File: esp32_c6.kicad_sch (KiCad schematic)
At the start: 1 part, among them U1 ESP32-WROOM-32

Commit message: ESP32S3 branch initial changes
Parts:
- removed U1: ESP32-WROOM-32, RF_Module:ESP32-WROOM-32, symbol RF_Module:ESP32-WROOM-32
- added C11, C3, C4: 100nf, Capacitor_SMD:C_0805_2012Metric, symbol Device:C
- added U1: ESP32-C6-DEVKITC-1-N8, kiC:MODULE_ESP32-C6-DEVKITC-1-N8, symbol ESP32-C6-DEVKITC-1-N8:ESP32-C6-DEVKITC-1-N8
- added U9: ESP32-C6-WROOM-1-N8, kiC:XCVR_ESP32-C6-WROOM-1-N8, symbol ESP32-C6-DEVKITC-1-N8:ESP32-C6-WROOM-1-N8
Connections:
- new net +3V3: C11.1, C3.1, C4.1, U1.J1_1 (ESP_3V3), U9.2 (3V3)
- new net +5V: U1.J1_14 (VCC_5V)
- new net EN: U1.J1_2 (CHIP_PU), U9.3 (EN)
- new net GND: C11.2, C3.2, C4.2, U1.J1_15 (GND_J1_15), U1.J3_1 (GND_J3_1), U1.J3_12 (GND_J3_12), U1.J3_15 (GND_J3_15), U9.1 (GND), U9.28 (GND), U9.29_1 (GND), U9.29_2 (GND), U9.29_3 (GND), U9.29_4 (GND), U9.29_5 (GND), U9.29_6 (GND), U9.29_7 (GND), U9.29_8 (GND), U9.29_9 (GND)
- new net IO_0: U1.J1_7 (GPIO0), U9.8 (IO0)
- new net IO_1: U1.J1_8 (GPIO1), U9.9 (IO1)
- new net IO_10: U1.J1_10 (GPIO10), U9.11 (IO10)
- new net IO_11: U1.J1_11 (GPIO11), U9.12 (IO11)
- new net IO_12: U1.J3_14 (GPIO12), U9.13 (IO12)
- new net IO_13: U1.J3_13 (GPIO13), U9.14 (IO13)
- new net IO_15: U1.J3_4 (GPIO15), U9.23 (IO15)
- new net IO_16: U9.25 (TXD0/GPIO16)
- new net IO_17: U9.24 (RXD0/GPIO17)
- new net IO_18: U1.J3_10 (GPIO18), U9.16 (IO18)
- new net IO_19: U1.J3_9 (GPIO19), U9.17 (IO19)
- new net IO_2: U1.J1_12 (GPIO2), U9.27 (IO2)
- new net IO_20: U1.J3_8 (GPIO20), U9.18 (IO20)
- new net IO_21: U1.J3_7 (GPIO21), U9.19 (IO21)
- new net IO_22: U1.J3_6 (GPIO22), U9.20 (IO22)
- new net IO_23: U1.J3_5 (GPIO23), U9.21 (IO23)
- new net IO_3: U1.J1_13 (GPIO3), U9.26 (IO3)
- new net IO_4: U1.J1_3 (GPIO4), U9.4 (IO4)
- new net IO_5: U1.J1_4 (GPIO5), U9.5 (IO5)
- new net IO_6: U1.J1_5 (GPIO6), U9.6 (IO6)
- new net IO_7: U1.J1_6 (GPIO7), U9.7 (IO7)
- new net IO_8: U1.J1_9 (GPIO8), U9.10 (IO8)
- new net IO_9: U1.J3_11 (GPIO9), U9.15 (IO9)
- new net MRX: U1.J3_3 (UART_RXD)
- new net MTX: U1.J3_2 (UART_TXD)

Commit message: Update KiCad project files
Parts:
- renumbered C3 to C1, C4 to C2, C11 to C3, U9 to U1, U1 to U2
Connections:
- net MRX is gone; now on net RXD0: U2.J3_3 (UART_RXD)
- net MTX is gone; now on net TXD0: U2.J3_2 (UART_TXD)
- net IO_16 renamed TXD0
- net IO_17 renamed RXD0
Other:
- moved on the sheet: C3, U1, U2

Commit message: Remove unused schematic files, lock files, and backup directories
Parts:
- added C10, C13, C14: 100n, Capacitor_SMD:C_0805_2012Metric, symbol Device:C
- added D10, D11, D9: LESD5D5.0CT1G, clackotron_fp:SOD-523_L1.2-W0.8-LS1.6-BI, symbol clackotronlib:LESD5D5.0CT1G
- added D12: ESD3.3, Diode_SMD:D_SOD-923, symbol Diode:ESD9B3.3ST5G
- added D8: 1N4148W, Diode_SMD:D_SOD-123, symbol Diode:1N4148W
- added J6: FT232RL, Connector_PinHeader_2.54mm:PinHeader_1x06_P2.54mm_Vertical, symbol Connector:Conn_01x06_Pin
- added Q4, Q5: Q_NPN_BCE, Package_TO_SOT_SMD:SOT-23W, symbol Device:Q_NPN_BCE
- added R15, R16, R20: 10k, Resistor_SMD:R_0805_2012Metric, symbol Device:R
- added R58, R59: 5.1k, Resistor_SMD:R_0805_2012Metric, symbol Device:R
- added SW1, SW2: SW_Push, Button_Switch_SMD:SW_Push_SPST_NO_Alps_SKRK, symbol Switch:SW_Push
- added SW11: boot, Button_Switch_SMD:SW_SPST_B3U-1000P, symbol Switch:SW_SPST
- added USBC1: USB3.1C16PFSMT, clackotron_fp:USB-C-SMD_TYPE-C-USB-17, symbol clackotronlib:USB3.1C16PFSMT
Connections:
- net +3V3: now also D8.1 (K)
- net EN: now also C10.1, C14.1, Q4.2 (C), R20.2, SW1.2
- net GND: now also C10.2, C13.2, C14.2, D10.1, D11.1, D12.1 (A1), D9.1, J6.6 (Pin_6), R58.1, R59.2, SW1.1, SW11.1 (A), SW2.1, USBC1.0, USBC1.A1 (GND), USBC1.A12 (GND)
- net IO_0: now also Q5.2 (C)
- net RXD0: now also J6.2 (Pin_2)
- net TXD0: now also J6.3 (Pin_3)
- new net: D8.2 (A), J6.4 (Pin_4)
- new net: Q5.1 (B), R16.2
- new net: R59.1, USBC1.A5 (CC1)
- new net: Q4.1 (B), R15.2
- new net: R58.2, USBC1.B5 (CC2)
- new net: D12.2 (A2), SW11.2 (B)
- new net +3.3V: R20.1
- new net CTS: J6.5 (Pin_5), Q4.3 (E), R16.1
- new net DTR: J6.1 (Pin_1), Q5.3 (E), R15.1
- new net GPIO0: C13.1, SW2.2
- new net USB2_D+: D10.2, USBC1.A7 (DN1), USBC1.B6 (DP2)
- new net USB2_D-: D9.2, USBC1.A6 (DP1), USBC1.B7 (DN2)
- new net VBUS: D11.2, USBC1.A4 (VBUS), USBC1.A9 (VBUS)
- no-connect marks 0 -> 2
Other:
- note added: "Automatic Bootloader"
- moved on the sheet: C1, C2, C3, U1, U2

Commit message: Update all schematic files and project
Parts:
- added C45, C46: 100nf, Capacitor_SMD:C_0805_2012Metric, symbol Device:C
- added J21: USB_B_Mini, kiC:USB_Mini-B_Lumberg_2486_01_Horizontal, symbol Connector:USB_B_Mini
- added L7: 100mh, Inductor_SMD:L_1206_3216Metric, symbol Device:L
- added R26, R37: 27, Resistor_SMD:R_0805_2012Metric, symbol Device:R
- added R62, R63: 5.1k, Resistor_SMD:R_0805_2012Metric, symbol Device:R
- added U9: LM1117DT-3.3, kiC:SOT-223-3_TabPin2, symbol Regulator_Linear:LM1117DT-3.3
- D10, D11, D9: footprint clackotron_fp:SOD-523_L1.2-W0.8-LS1.6-BI -> Diode_SMD:D_SOD-523
- SW11: footprint Button_Switch_SMD:SW_SPST_B3U-1000P -> Button_Switch_SMD:SW_Push_SPST_NO_Alps_SKRK
- USBC1: footprint clackotron_fp:USB-C-SMD_TYPE-C-USB-17 -> kiC:USB-C-SMD_TYPE-C-USB-17
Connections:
- net +3V3: now also C46.2, U9.2 (VO)
- net GND: now also C45.1, C46.1, J21.5 (GND1), J21.6 (Shield), U9.1 (GND1)
- net IO_12: now also R37.1, R63.1
- net IO_13: now also R26.1, R62.1
- net USB2_D+: now also R62.2
- net USB2_D-: now also R63.2
- net VBUS: now also J21.1 (VBUS), L7.1
- net GPIO9: now reaches D12.2 (A2), SW11.2 (B)
- new net: J21.2 (D-), R37.2
- new net: J21.3 (D+), R26.2
- new net: C45.2, L7.2, U9.3 (VI)
- new net ID_USB: J21.4 (ID)
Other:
- moved on the sheet: D11, D12, SW11

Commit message: Update all schematic files and project
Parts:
- removed SW2: SW_Push, Button_Switch_SMD:SW_Push_SPST_NO_Alps_SKRK, symbol Switch:SW_Push
- added C49: 100nf, Capacitor_SMD:C_1206_3216Metric, symbol Device:C
- added C50, C51: 100n, Capacitor_SMD:C_0805_2012Metric, symbol Device:C
- added D14: 1N5819, Diode_SMD:D_2512_6332Metric, symbol Diode:1N5819
- added J22: JTAG, Connector_PinHeader_1.27mm:PinHeader_1x06_P1.27mm_Vertical, symbol Connector:Conn_01x06_Pin
- added R64: 10K, Resistor_SMD:R_0805_2012Metric, symbol Device:R
- added Y2: Crystal, Crystal:Crystal_SMD_EuroQuartz_EQ161-2Pin_3.2x1.5mm, symbol Device:Crystal
- C45: footprint Capacitor_SMD:C_0805_2012Metric -> Capacitor_SMD:C_1206_3216Metric
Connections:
- net GPIO0 is gone; now on net GPIO9: C13.1
- net +3V3: now also J22.1 (Pin_1), R64.1
- net +5V: now also C45.2, L7.2, U9.3 (VI), C49.2
- net GND: now also C49.1, C50.2, C51.2, J22.6 (Pin_6)
- net IO_0: now also C50.1, Y2.1
- net IO_1: now also C51.1, Y2.2
- net IO_4: now also J22.2 (Pin_2)
- net IO_5: now also J22.3 (Pin_3)
- net IO_6: now also J22.4 (Pin_4)
- net IO_7: now also J22.5 (Pin_5)
- net IO_8: now also R64.2
- net VBUS: now also D14.2 (A); no longer L7.1
- new net: D14.1 (K), L7.1
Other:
- moved on the sheet: D12, SW11, U1, U2

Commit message: Update schematics, PCB, and project files
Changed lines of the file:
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@@
 		(color 0 0 0 0)
 	)
-	(junction
-		(at 64.77 119.38)
-		(diameter 0)
-		(color 0 0 0 0)
-	)
 	(no_connect
 		(at 113.665 50.8)
@@
 	(wire
 		(pts
-			(xy 62.23 119.38) (xy 64.77 119.38)
-		)
-		(stroke
-			(width 0)
-			(type default)
-		)
-	)
-	(wire
-		(pts
 			(xy 228.6 219.71) (xy 240.03 219.71)
 		)
@@
 	(wire
 		(pts
-			(xy 246.38 93.98) (xy 243.84 93.98)
-		)
-		(stroke
-			(width 0)
-			(type default)
-		)
-	)
-	(wire
-		(pts
 			(xy 84.455 53.34) (xy 84.455 59.69)
 		)
@@
 	(wire
 		(pts
-			(xy 64.77 116.84) (xy 64.77 119.38)
+			(xy 133.35 209.55) (xy 133.35 210.82)
 		)
 		(stroke
@@
 	(wire
 		(pts
-			(xy 133.35 209.55) (xy 133.35 210.82)
+			(xy 246.38 147.32) (xy 243.84 147.32)
 		)
 		(stroke
@@
 	(wire
 		(pts
-			(xy 246.38 147.32) (xy 243.84 147.32)
+			(xy 91.44 168.91) (xy 105.41 168.91)
 		)
 		(stroke
@@
 	(wire
 		(pts
-			(xy 91.44 168.91) (xy 105.41 168.91)
+			(xy 142.24 58.42) (xy 142.24 60.96)
 		)
 		(stroke
@@
 	(wire
 		(pts
-			(xy 142.24 58.42) (xy 142.24 60.96)
+			(xy 354.33 199.39) (xy 354.33 203.2)
 		)
 		(stroke
@@
 	(wire
 		(pts
-			(xy 354.33 200.66) (xy 354.33 203.2)
+			(xy 127 133.35) (xy 148.59 133.35)
 		)
 		(stroke
@@
 	(wire
 		(pts
-			(xy 127 133.35) (xy 148.59 133.35)
+			(xy 64.77 116.84) (xy 64.77 121.92)
 		)
 		(stroke
@@
 	(wire
 		(pts
-			(xy 62.23 116.84) (xy 62.23 119.38)
+			(xy 62.23 116.84) (xy 62.23 123.19)
 		)
 		(stroke
@@
 	(wire
 		(pts
-			(xy 246.38 129.54) (xy 243.84 129.54)
-		)
-		(stroke
-			(width 0)
-			(type default)
-		)
-	)
-	(wire
-		(pts
 			(xy 130.81 209.55) (xy 133.35 209.55)
 		)
@@
 	(wire
 		(pts
-			(xy 246.38 127) (xy 243.84 127)
-		)
-		(stroke
-			(width 0)
-			(type default)
-		)
-	)
-	(wire
-		(pts
 			(xy 82.55 101.6) (xy 72.39 101.6)
 		)
@@
 	(wire
 		(pts
-			(xy 64.77 119.38) (xy 64.77 121.92)
-		)
-		(stroke
-			(width 0)
-			(type default)
-		)
-	)
-	(wire
-		(pts
 			(xy 144.78 128.27) (xy 148.59 128.27)
 		)
@@
 		)
 	)
-	(label "EN"
-		(at 243.84 93.98 180)
-		(effects
-			(font
-				(size 1.27 1.27)
-			)
-			(justify right bottom)
-		)
-	)
 	(label "IO_15"
 		(at 191.77 118.11 0)
@@
 		)
 	)
-	(label "IO_12"
-		(at 243.84 127 180)
-		(effects
-			(font
-				(size 1.27 1.27)
-			)
-			(justify right bottom)
-		)
-	)
 	(label "IO_19"
 		(at 243.84 142.24 180)
@@
 		)
 	)
-	(label "IO_13"
-		(at 243.84 129.54 180)
-		(effects
-			(font
-				(size 1.27 1.27)
-			)
-			(justify right bottom)
-		)
-	)
 	(label "IO_0"
 		(at 243.84 96.52 180)
@@
 		)
 	)
-	(hierarchical_label "IO_12"
-		(shape input)
-		(at 246.38 127 0)
-		(effects
-			(font
-				(size 1.27 1.27)
-			)
-			(justify left)
-		)
-	)
-	(hierarchical_label "IO_13"
-		(shape input)
-		(at 246.38 129.54 0)
-		(effects
-			(font
-				(size 1.27 1.27)
-			)
-			(justify left)
-		)
-	)
 	(hierarchical_label "CTS"
 		(shape input)
@@
 		)
 	)
-	(hierarchical_label "EN"
-		(shape input)
-		(at 246.38 93.98 0)
-		(effects
-			(font
-				(size 1.27 1.27)
-			)
-			(justify left)
-		)
-	)
 	(hierarchical_label "DTR"
 		(shape input)
@@
 	(symbol
 		(lib_id "power:+3.3V")
-		(at 354.33 200.66 0)
+		(at 354.33 199.39 0)
 		(unit 1)
 		(body_style 1)
@@
 		(dnp no)
 		(property "Reference" "#PWR029"
-			(at 354.33 204.47 0)
+			(at 354.33 203.2 0)
 			(hide yes)
 			(show_name no)
@@
 		)
 		(property "Value" "+3.3V"
-			(at 355.6 196.85 0)
+			(at 355.6 195.58 0)
 			(show_name no)
 			(do_not_autoplace no)
@@
 		)
 		(property "Footprint" ""
-			(at 354.33 200.66 0)
+			(at 354.33 199.39 0)
 			(hide yes)
 			(show_name no)
@@
 		)
 		(property "Datasheet" ""
-			(at 354.33 200.66 0)
+			(at 354.33 199.39 0)
 			(hide yes)
 			(show_name no)
@@
 		)
 		(property "Description" ""
-			(at 354.33 200.66 0)
+			(at 354.33 199.39 0)
 			(show_name no)
 			(do_not_autoplace no)
@@
 		(in_pos_files yes)
 		(dnp no)
-		(fields_autoplaced yes)
 		(property "Reference" "#PWR0137"
 			(at 64.77 128.27 0)
@@
 		)
 		(property "Value" "GND"
-			(at 64.77 126.365 0)
+			(at 66.802 126.238 0)
 			(show_name no)
 			(do_not_autoplace no)
@@
 					(unit 1)
 				)
+			)
+		)
+	)
+	(symbol
+		(lib_id "power:GND")
+		(at 62.23 123.19 0)
+		(unit 1)
+		(body_style 1)
+		(exclude_from_sim no)
+		(in_bom yes)
+		(on_board yes)
+		(in_pos_files yes)
+		(dnp no)
+		(fields_autoplaced yes)
+		(property "Reference" "#PWR0140"
+			(at 62.23 129.54 0)
+			(hide yes)
+			(show_name no)
+			(do_not_autoplace no)
+			(effects
+				(font
+					(size 1.27 1.27)
+				)
+			)
+		)
+		(property "Value" "GND"
+			(at 62.23 127.635 0)
+			(show_name no)
+			(do_not_autoplace no)
+			(effects
+				(font
+					(size 1.27 1.27)
+				)
+			)
+		)
+		(property "Footprint" ""
+			(at 62.23 123.19 0)
+			(hide yes)
+			(show_name no)
+			(do_not_autoplace no)
+			(effects
+				(font
+					(size 1.27 1.27)
+				)
+			)
+		)
+		(property "Datasheet" ""
+			(at 62.23 123.19 0)
+			(hide yes)
+			(show_name no)
+			(do_not_autoplace no)
+			(effects
+				(font
+					(size 1.27 1.27)
+				)
+			)
+		)
+		(property "Description" ""
+			(at 62.23 123.19 0)
+			(show_name no)
+			(do_not_autoplace no)
+			(effects
+				(font
+					(size 1.27 1.27)
+				)
+			)
+		)
+		(pin "1"
+		)
+		(instances
+			(project "esp32_xiaozhi"
+				(path "/cae338e8-f342-43cb-b99a-a0486629133c/99dbbdf2-0f67-4248-a995-74d5ebf0be3f"
+					(reference "#PWR0140")
+					(unit 1)
+				)

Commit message: Actualización de esquema y PCB del proyecto ESP32C6 Xiaozhi
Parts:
- C49: footprint Capacitor_SMD:C_1206_3216Metric -> Capacitor_SMD:C_0805_2012Metric
- SW1, SW11: footprint Button_Switch_SMD:SW_Push_SPST_NO_Alps_SKRK -> Button_Switch_SMD:SW_Push_1P1T_XKB_TS-1187A
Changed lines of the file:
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@@
 	(wire
 		(pts
+			(xy 46.99 166.37) (xy 46.99 161.29)
+		)
+		(stroke
+			(width 0)
+			(type default)
+		)
+	)
+	(wire
+		(pts
 			(xy 228.6 217.17) (xy 232.41 217.17)
 		)
@@
 	(wire
 		(pts
-			(xy 354.33 199.39) (xy 354.33 203.2)
+			(xy 354.33 198.12) (xy 354.33 203.2)
 		)
 		(stroke
@@
 			)
 		)
-		(property "Footprint" "Button_Switch_SMD:SW_Push_SPST_NO_Alps_SKRK"
+		(property "Footprint" "Button_Switch_SMD:SW_Push_1P1T_XKB_TS-1187A"
 			(at 85.09 203.2 0)
 			(hide yes)
@@
 	(symbol
 		(lib_id "power:+3.3V")
-		(at 354.33 199.39 0)
+		(at 354.33 198.12 0)
 		(unit 1)
 		(body_style 1)
@@
 		(dnp no)
 		(property "Reference" "#PWR029"
-			(at 354.33 203.2 0)
+			(at 354.33 201.93 0)
 			(hide yes)
 			(show_name no)
@@
 		)
 		(property "Value" "+3.3V"
-			(at 355.6 195.58 0)
+			(at 355.6 194.31 0)
 			(show_name no)
 			(do_not_autoplace no)
@@
 		)
 		(property "Footprint" ""
-			(at 354.33 199.39 0)
+			(at 354.33 198.12 0)
 			(hide yes)
 			(show_name no)
@@
 		)
 		(property "Datasheet" ""
-			(at 354.33 199.39 0)
+			(at 354.33 198.12 0)
 			(hide yes)
 			(show_name no)
@@
 		)
 		(property "Description" ""
-			(at 354.33 199.39 0)
+			(at 354.33 198.12 0)
 			(show_name no)
 			(do_not_autoplace no)
@@
 	(symbol
 		(lib_id "power:GND")
-		(at 46.99 161.29 0)
+		(at 46.99 166.37 0)
 		(unit 1)
 		(body_style 1)
@@
 		(dnp no)
 		(property "Reference" "#PWR025"
-			(at 46.99 167.64 0)
+			(at 46.99 172.72 0)
 			(hide yes)
 			(show_name no)
@@
 		)
 		(property "Value" "GND"
-			(at 50.546 162.814 0)
+			(at 50.546 167.894 0)
 			(show_name no)
 			(do_not_autoplace no)
@@
 		)
 		(property "Footprint" ""
-			(at 46.99 161.29 0)
+			(at 46.99 166.37 0)
 			(hide yes)
 			(show_name no)
@@
 		)
 		(property "Datasheet" ""
-			(at 46.99 161.29 0)
+			(at 46.99 166.37 0)
 			(hide yes)
 			(show_name no)
@@
 		)
 		(property "Description" "Power symbol creates a global label with name \"GND\" , ground"
-			(at 46.99 161.29 0)
+			(at 46.99 166.37 0)
 			(hide yes)
 			(show_name no)
@@
 			)
 		)
-		(property "Footprint" "Button_Switch_SMD:SW_Push_SPST_NO_Alps_SKRK"
+		(property "Footprint" "Button_Switch_SMD:SW_Push_1P1T_XKB_TS-1187A"
 			(at 125.73 209.55 0)
 			(hide yes)
@@
 			)
 		)
-		(property "Footprint" "Capacitor_SMD:C_1206_3216Metric"
+		(property "Footprint" "Capacitor_SMD:C_0805_2012Metric"
 			(at 181.9148 48.26 0)
 			(hide yes)

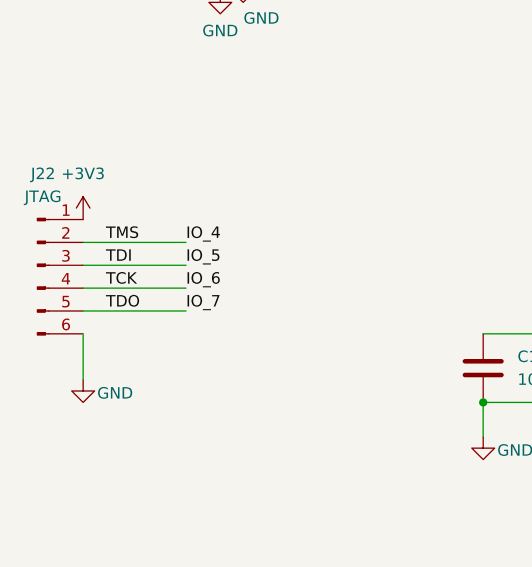
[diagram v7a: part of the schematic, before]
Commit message: Actualizaciones para versión single ESP32C6
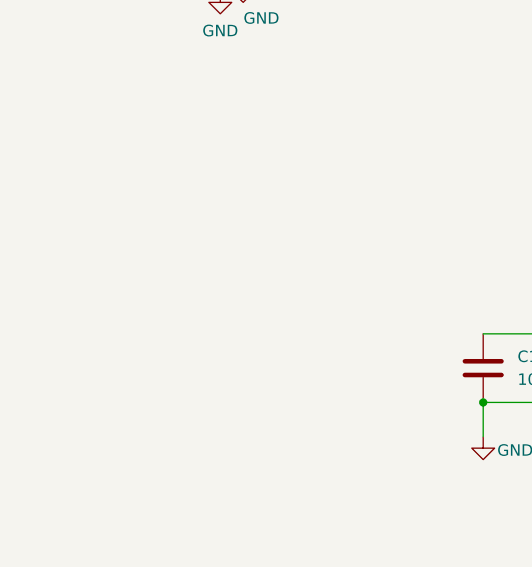
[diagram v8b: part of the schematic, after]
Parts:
- removed J22: JTAG, Connector_PinHeader_1.27mm:PinHeader_1x06_P1.27mm_Vertical, symbol Connector:Conn_01x06_Pin
- U9: footprint kiC:SOT-223-3_TabPin2 -> kiC:TO-252-3_TabPin2
